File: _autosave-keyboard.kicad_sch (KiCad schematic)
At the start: 0 parts

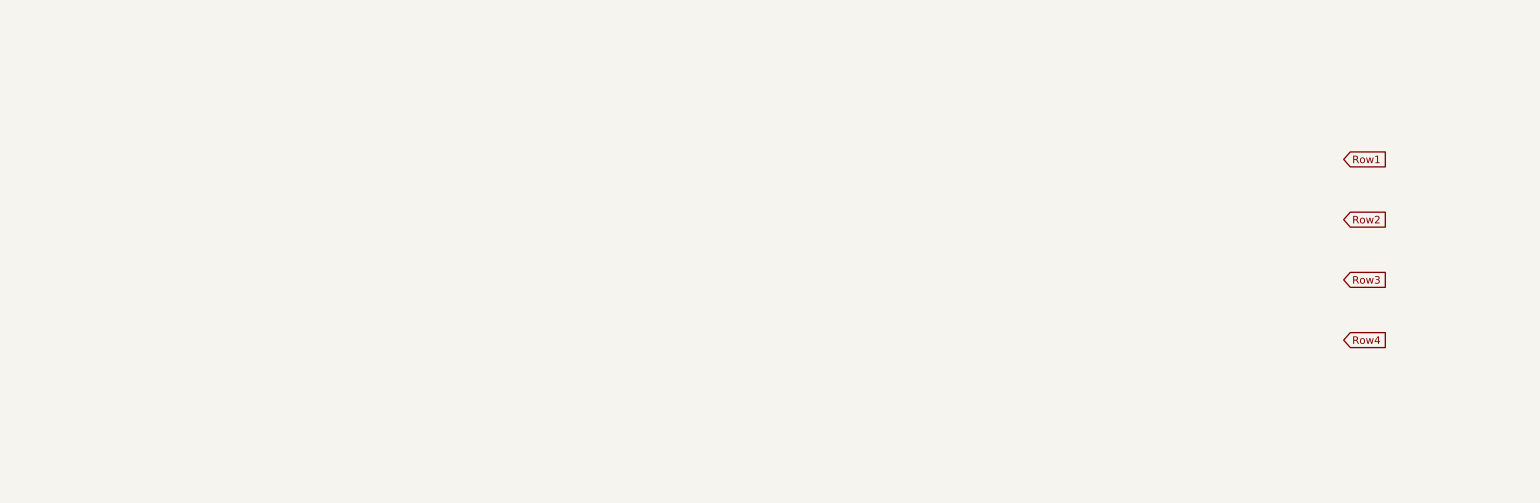
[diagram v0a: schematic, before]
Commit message: updated layout
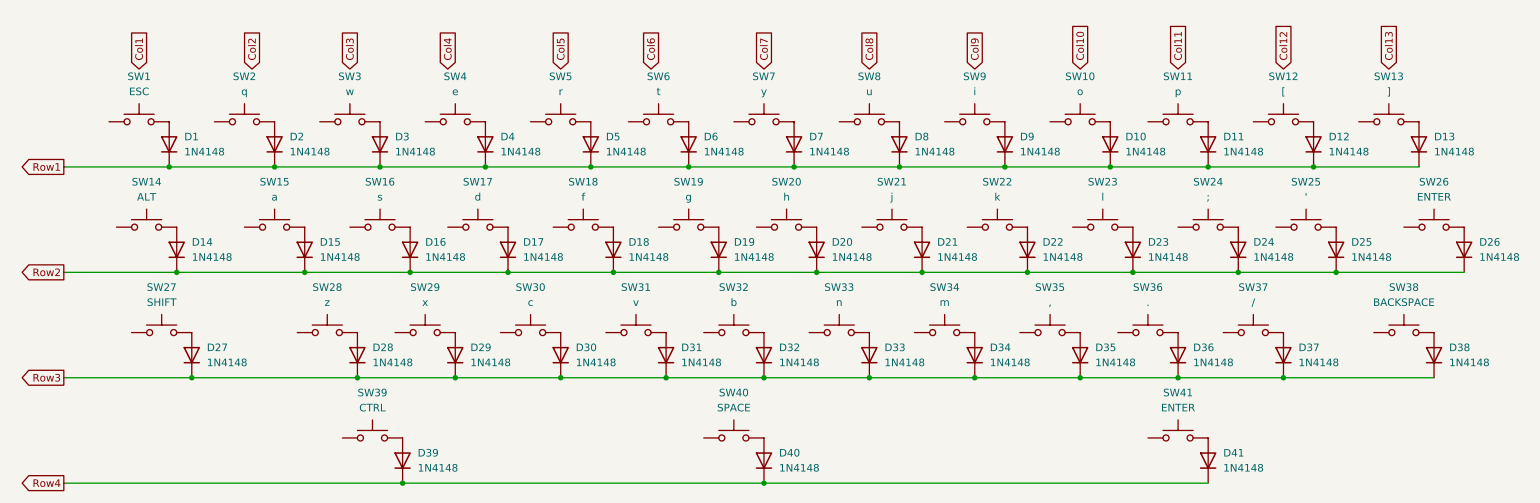
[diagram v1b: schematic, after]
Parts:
- added D1, D10, D11, D12, D13, D14, D15, D16, D17, D18, D19, D2, D20, D21, D22, D23, D24, D25, D26, D27, D28, D29, D3, D30, D31, D32, D33, D34, D35, D36, D37, D38, D39, D4, D40, D41, D5, D6, D7, D8, D9: 1N4148, Diode_THT:D_DO-35_SOD27_P7.62mm_Horizontal, symbol Diode:1N4148
- added SW1: ESC, symbol Switch:SW_MEC_5G
- added SW10: o, symbol Switch:SW_MEC_5G
- added SW11: p, symbol Switch:SW_MEC_5G
- added SW12: [, symbol Switch:SW_MEC_5G
- added SW13: ], symbol Switch:SW_MEC_5G
- added SW14: ALT, symbol Switch:SW_MEC_5G
- added SW15: a, symbol Switch:SW_MEC_5G
- added SW16: s, symbol Switch:SW_MEC_5G
- added SW17: d, symbol Switch:SW_MEC_5G
- added SW18: f, symbol Switch:SW_MEC_5G
- added SW19: g, symbol Switch:SW_MEC_5G
- added SW2: q, symbol Switch:SW_MEC_5G
- added SW20: h, symbol Switch:SW_MEC_5G
- added SW21: j, symbol Switch:SW_MEC_5G
- added SW22: k, symbol Switch:SW_MEC_5G
- added SW23: l, symbol Switch:SW_MEC_5G
- added SW24: ;, symbol Switch:SW_MEC_5G
- added SW25: ', symbol Switch:SW_MEC_5G
- added SW26, SW41: ENTER, symbol Switch:SW_MEC_5G
- added SW27: SHIFT, symbol Switch:SW_MEC_5G
- added SW28: z, symbol Switch:SW_MEC_5G
- added SW29: x, symbol Switch:SW_MEC_5G
- added SW3: w, symbol Switch:SW_MEC_5G
- added SW30: c, symbol Switch:SW_MEC_5G
- added SW31: v, symbol Switch:SW_MEC_5G
- added SW32: b, symbol Switch:SW_MEC_5G
- added SW33: n, symbol Switch:SW_MEC_5G
- added SW34: m, symbol Switch:SW_MEC_5G
- added SW35: ,, symbol Switch:SW_MEC_5G
- added SW36: ., symbol Switch:SW_MEC_5G
- added SW37: /, symbol Switch:SW_MEC_5G
- added SW38: BACKSPACE, symbol Switch:SW_MEC_5G
- added SW39: CTRL, symbol Switch:SW_MEC_5G
- added SW4: e, symbol Switch:SW_MEC_5G
- added SW40: SPACE, symbol Switch:SW_MEC_5G
- added SW5: r, symbol Switch:SW_MEC_5G
- added SW6: t, symbol Switch:SW_MEC_5G
- added SW7: y, symbol Switch:SW_MEC_5G
- added SW8: u, symbol Switch:SW_MEC_5G
- added SW9: i, symbol Switch:SW_MEC_5G
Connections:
- net Row1: now also D1.1 (K), D10.1 (K), D11.1 (K), D12.1 (K), D13.1 (K), D2.1 (K), D3.1 (K), D4.1 (K), D5.1 (K), D6.1 (K), D7.1 (K), D8.1 (K), D9.1 (K)
- net Row2: now also D14.1 (K), D15.1 (K), D16.1 (K), D17.1 (K), D18.1 (K), D19.1 (K), D20.1 (K), D21.1 (K), D22.1 (K), D23.1 (K), D24.1 (K), D25.1 (K), D26.1 (K)
- net Row3: now also D27.1 (K), D28.1 (K), D29.1 (K), D30.1 (K), D31.1 (K), D32.1 (K), D33.1 (K), D34.1 (K), D35.1 (K), D36.1 (K), D37.1 (K), D38.1 (K)
- net Row4: now also D39.1 (K), D40.1 (K), D41.1 (K)
- new net: D28.2 (A), SW28.3 (B), SW28.4 (B)
- new net: SW36.1 (A), SW36.2 (A)
- new net: D36.2 (A), SW36.3 (B), SW36.4 (B)
- new net: SW4.1 (A), SW4.2 (A)
- new net: D4.2 (A), SW4.3 (B), SW4.4 (B)
- new net: D9.2 (A), SW9.3 (B), SW9.4 (B)
- new net: SW19.1 (A), SW19.2 (A)
- new net: D19.2 (A), SW19.3 (B), SW19.4 (B)
- new net: SW38.1 (A), SW38.2 (A)
- new net: D38.2 (A), SW38.3 (B), SW38.4 (B)
- new net: SW28.1 (A), SW28.2 (A)
- new net: SW13.1 (A), SW13.2 (A)
- new net: D13.2 (A), SW13.3 (B), SW13.4 (B)
- new net: SW21.1 (A), SW21.2 (A)
- new net: D21.2 (A), SW21.3 (B), SW21.4 (B)
- new net: SW11.1 (A), SW11.2 (A)
- new net: D11.2 (A), SW11.3 (B), SW11.4 (B)
- new net: D15.2 (A), SW15.3 (B), SW15.4 (B)
- new net: D10.2 (A), SW10.3 (B), SW10.4 (B)
- new net: SW9.1 (A), SW9.2 (A)
- new net: D29.2 (A), SW29.3 (B), SW29.4 (B)
- new net: SW27.1 (A), SW27.2 (A)
- new net: D27.2 (A), SW27.3 (B), SW27.4 (B)
- new net: D3.2 (A), SW3.3 (B), SW3.4 (B)
- new net: D31.2 (A), SW31.3 (B), SW31.4 (B)
- new net: D41.2 (A), SW41.3 (B), SW41.4 (B)
- new net: SW20.1 (A), SW20.2 (A)
- new net: D20.2 (A), SW20.3 (B), SW20.4 (B)
- new net: D23.2 (A), SW23.3 (B), SW23.4 (B)
- new net: SW24.1 (A), SW24.2 (A)
- new net: D24.2 (A), SW24.3 (B), SW24.4 (B)
- new net: SW3.1 (A), SW3.2 (A)
- new net: D18.2 (A), SW18.3 (B), SW18.4 (B)
- new net: SW37.1 (A), SW37.2 (A)
- new net: D37.2 (A), SW37.3 (B), SW37.4 (B)
- new net: SW5.1 (A), SW5.2 (A)
- new net: D5.2 (A), SW5.3 (B), SW5.4 (B)
- new net: SW35.1 (A), SW35.2 (A)
- new net: D35.2 (A), SW35.3 (B), SW35.4 (B)
- new net: SW30.1 (A), SW30.2 (A)
- new net: D30.2 (A), SW30.3 (B), SW30.4 (B)
- new net: SW26.1 (A), SW26.2 (A)
- new net: D26.2 (A), SW26.3 (B), SW26.4 (B)
- new net: SW15.1 (A), SW15.2 (A)
- new net: SW17.1 (A), SW17.2 (A)
- new net: D17.2 (A), SW17.3 (B), SW17.4 (B)
- new net: D34.2 (A), SW34.3 (B), SW34.4 (B)
- new net: D12.2 (A), SW12.3 (B), SW12.4 (B)
- new net: D22.2 (A), SW22.3 (B), SW22.4 (B)
- new net: SW1.1 (A), SW1.2 (A)
- new net: D1.2 (A), SW1.3 (B), SW1.4 (B)
- new net: D25.2 (A), SW25.3 (B), SW25.4 (B)
- new net: D40.2 (A), SW40.3 (B), SW40.4 (B)
- new net: D8.2 (A), SW8.3 (B), SW8.4 (B)
- new net: SW10.1 (A), SW10.2 (A)
- new net: SW31.1 (A), SW31.2 (A)
- new net: D16.2 (A), SW16.3 (B), SW16.4 (B)
- new net: SW39.1 (A), SW39.2 (A)
- new net: D39.2 (A), SW39.3 (B), SW39.4 (B)
- new net: D32.2 (A), SW32.3 (B), SW32.4 (B)
- new net: SW22.1 (A), SW22.2 (A)
- new net: SW2.1 (A), SW2.2 (A)
- new net: D2.2 (A), SW2.3 (B), SW2.4 (B)
- new net: SW18.1 (A), SW18.2 (A)
- new net: D14.2 (A), SW14.3 (B), SW14.4 (B)
- new net: SW6.1 (A), SW6.2 (A)
- new net: D6.2 (A), SW6.3 (B), SW6.4 (B)
- new net: SW41.1 (A), SW41.2 (A)
- new net: SW40.1 (A), SW40.2 (A)
- new net: SW33.1 (A), SW33.2 (A)
- new net: D33.2 (A), SW33.3 (B), SW33.4 (B)
- new net: D7.2 (A), SW7.3 (B), SW7.4 (B)
- new net: SW23.1 (A), SW23.2 (A)
- new net: SW8.1 (A), SW8.2 (A)
- new net: SW34.1 (A), SW34.2 (A)
- new net: SW14.1 (A), SW14.2 (A)
- new net: SW29.1 (A), SW29.2 (A)
- new net: SW7.1 (A), SW7.2 (A)
- new net: SW25.1 (A), SW25.2 (A)
- new net: SW12.1 (A), SW12.2 (A)
- new net: SW16.1 (A), SW16.2 (A)
- new net: SW32.1 (A), SW32.2 (A)
